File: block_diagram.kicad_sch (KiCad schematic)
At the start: 0 parts

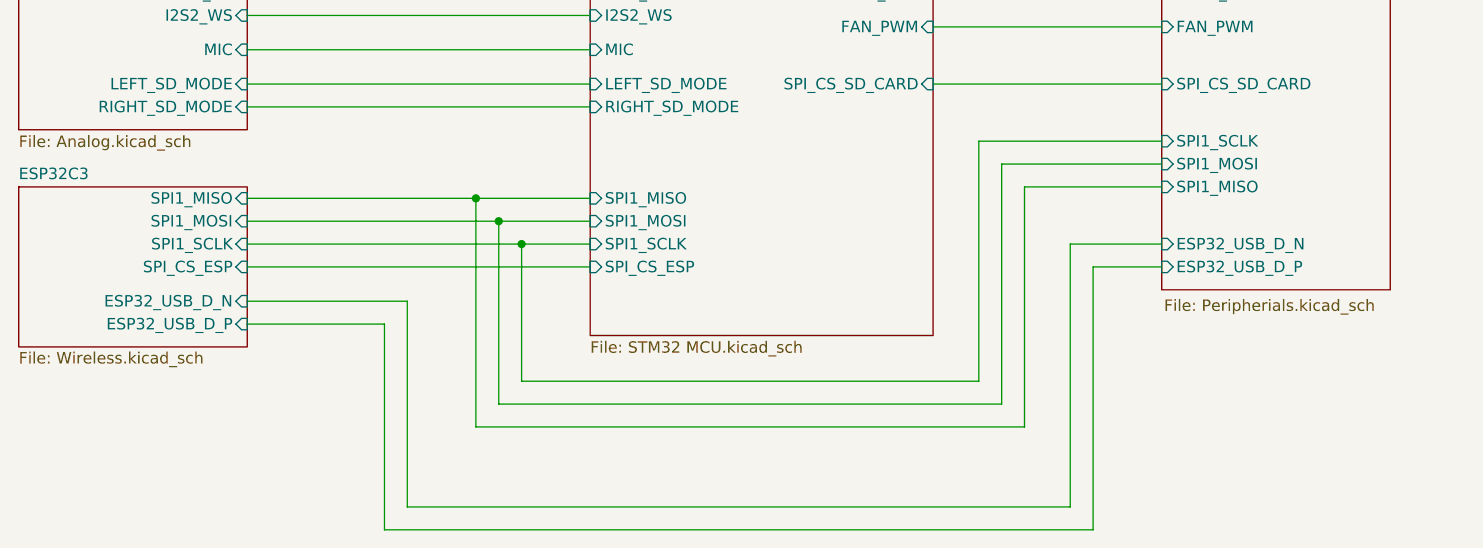
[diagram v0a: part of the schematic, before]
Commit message: got rid of usb
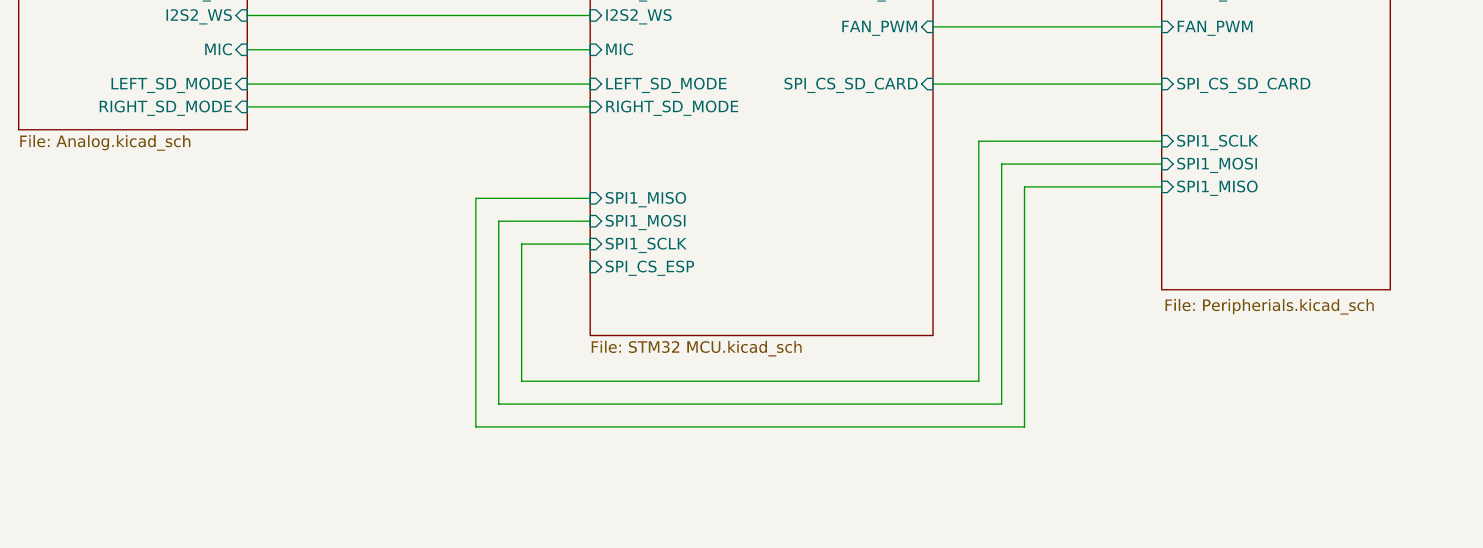
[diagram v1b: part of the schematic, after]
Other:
- removed sheet ESP32C3
- sheet Peripherials ports: added none; removed ESP32_USB_D_N, ESP32_USB_D_P
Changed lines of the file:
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@@
-	)
-	(junction
-		(at 115.57 127)
-		(diameter 0)
-		(color 0 0 0 0)
 	)
 	(junction
@@
 		(color 0 0 0 0)
 	)
-	(junction
-		(at 113.03 124.46)
-		(diameter 0)
-		(color 0 0 0 0)
-	)
-	(junction
-		(at 118.11 129.54)
-		(diameter 0)
-		(color 0 0 0 0)
-	)
 	(wire
 		(pts
@@
 	(wire
 		(pts
-			(xy 102.87 138.43) (xy 102.87 161.29)
-		)
-		(stroke
-			(width 0)
-			(type default)
-		)
-	)
-	(wire
-		(pts
 			(xy 175.26 19.05) (xy 116.84 19.05)
 		)
@@
 	(wire
 		(pts
-			(xy 105.41 135.89) (xy 87.63 135.89)
-		)
-		(stroke
-			(width 0)
-			(type default)
-		)
-	)
-	(wire
-		(pts
 			(xy 163.83 101.6) (xy 189.23 101.6)
 		)
@@
 	(wire
 		(pts
+			(xy 113.03 124.46) (xy 125.73 124.46)
+		)
+		(stroke
+			(width 0)
+			(type default)
+		)
+	)
+	(wire
+		(pts
 			(xy 114.3 16.51) (xy 114.3 38.1)
 		)
@@
 	(wire
 		(pts
-			(xy 87.63 132.08) (xy 125.73 132.08)
-		)
-		(stroke
-			(width 0)
-			(type default)
-		)
-	)
-	(wire
-		(pts
 			(xy 87.63 62.23) (xy 125.73 62.23)
 		)
@@
 	(wire
 		(pts
+			(xy 118.11 129.54) (xy 125.73 129.54)
+		)
+		(stroke
+			(width 0)
+			(type default)
+		)
+	)
+	(wire
+		(pts
 			(xy 116.84 19.05) (xy 116.84 35.56)
 		)
@@
 	(wire
 		(pts
-			(xy 87.63 124.46) (xy 125.73 124.46)
-		)
-		(stroke
-			(width 0)
-			(type default)
-		)
-	)
-	(wire
-		(pts
-			(xy 105.41 158.75) (xy 105.41 135.89)
-		)
-		(stroke
-			(width 0)
-			(type default)
-		)
-	)
-	(wire
-		(pts
 			(xy 113.03 149.86) (xy 113.03 124.46)
 		)
@@
 	(wire
 		(pts
-			(xy 189.23 129.54) (xy 179.07 129.54)
-		)
-		(stroke
-			(width 0)
-			(type default)
-		)
-	)
-	(wire
-		(pts
 			(xy 189.23 123.19) (xy 173.99 123.19)
 		)
@@
 	(wire
 		(pts
-			(xy 87.63 127) (xy 125.73 127)
-		)
-		(stroke
-			(width 0)
-			(type default)
-		)
-	)
-	(wire
-		(pts
 			(xy 163.83 76.2) (xy 189.23 76.2)
 		)
@@
 	(wire
 		(pts
-			(xy 102.87 161.29) (xy 181.61 161.29)
-		)
-		(stroke
-			(width 0)
-			(type default)
-		)
-	)
-	(wire
-		(pts
 			(xy 163.83 68.58) (xy 189.23 68.58)
 		)
@@
 	(wire
 		(pts
-			(xy 181.61 132.08) (xy 189.23 132.08)
-		)
-		(stroke
-			(width 0)
-			(type default)
-		)
-	)
-	(wire
-		(pts
 			(xy 115.57 147.32) (xy 115.57 127)
 		)
@@
 	(wire
 		(pts
-			(xy 87.63 129.54) (xy 125.73 129.54)
-		)
-		(stroke
-			(width 0)
-			(type default)
-		)
-	)
-	(wire
-		(pts
 			(xy 168.91 144.78) (xy 168.91 118.11)
 		)
@@
 	(wire
 		(pts
-			(xy 181.61 161.29) (xy 181.61 132.08)
-		)
-		(stroke
-			(width 0)
-			(type default)
-		)
-	)
-	(wire
-		(pts
 			(xy 163.83 73.66) (xy 189.23 73.66)
 		)
@@
 	(wire
 		(pts
-			(xy 179.07 158.75) (xy 105.41 158.75)
-		)
-		(stroke
-			(width 0)
-			(type default)
-		)
-	)
-	(wire
-		(pts
 			(xy 163.83 55.88) (xy 189.23 55.88)
 		)
@@
 	(wire
 		(pts
-			(xy 87.63 138.43) (xy 102.87 138.43)
+			(xy 115.57 127) (xy 125.73 127)
 		)
 		(stroke
@@
 		(pts
 			(xy 189.23 35.56) (xy 175.26 35.56)
-		)
-		(stroke
-			(width 0)
-			(type default)
-		)
-	)
-	(wire
-		(pts
-			(xy 179.07 129.54) (xy 179.07 158.75)
 		)
 		(stroke
@@
 	)
 	(sheet
-		(at 62.23 123.19)
-		(size 25.4 17.78)
-		(exclude_from_sim no)
-		(in_bom yes)
-		(on_board yes)
-		(dnp no)
-		(stroke
-			(width 0.1524)
-			(type solid)
-		)
-		(fill
-			(color 0 0 0 0)
-		)
-		(property "Sheetname" "ESP32C3"
-			(at 62.23 122.4784 0)
-			(show_name no)
-			(do_not_autoplace no)
-			(effects
-				(font
-					(size 1.27 1.27)
-				)
-				(justify left bottom)
-			)
-		)
-		(property "Sheetfile" "Wireless.kicad_sch"
-			(at 62.23 141.478 0)
-			(show_name no)
-			(do_not_autoplace no)
-			(effects
-				(font
-					(size 1.27 1.27)
-				)
-				(justify left top)
-			)
-		)
-		(pin "ESP32_USB_D_N" input
-			(at 87.63 135.89 0)
-			(effects
-				(font
-					(size 1.27 1.27)
-				)
-				(justify right)
-			)
-		)
-		(pin "ESP32_USB_D_P" input
-			(at 87.63 138.43 0)
-			(effects
-				(font
-					(size 1.27 1.27)
-				)
-				(justify right)
-			)
-		)
-		(pin "SPI1_MISO" input
-			(at 87.63 124.46 0)
-			(effects
-				(font
-					(size 1.27 1.27)
-				)
-				(justify right)
-			)
-		)
-		(pin "SPI1_MOSI" input
-			(at 87.63 127 0)
-			(effects
-				(font
-					(size 1.27 1.27)
-				)
-				(justify right)
-			)
-		)
-		(pin "SPI1_SCLK" input
-			(at 87.63 129.54 0)
-			(effects
-				(font
-					(size 1.27 1.27)
-				)
-				(justify right)
-			)
-		)
-		(pin "SPI_CS_ESP" input
-			(at 87.63 132.08 0)
-			(effects
-				(font
-					(size 1.27 1.27)
-				)
-				(justify right)
-			)
-		)
-		(instances
-			(project "SeniorDesign_PCB"
-				(path "/88e1ced0-9576-4565-ab29-f74bf51ccbda"
-					(page "7")
-				)
-			)
-		)
-	)
-	(sheet
 		(at 62.23 25.4)
 		(size 25.4 16.51)
@@
 			)
 		)
-		(pin "ESP32_USB_D_N" input
-			(at 189.23 129.54 180)
-			(effects
-				(font
-					(size 1.27 1.27)
-				)
-				(justify left)
-			)
-		)
-		(pin "ESP32_USB_D_P" input
-			(at 189.23 132.08 180)
-			(effects
-				(font
-					(size 1.27 1.27)
-				)
-				(justify left)
-			)
-		)
